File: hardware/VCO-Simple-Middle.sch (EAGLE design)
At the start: 14 parts

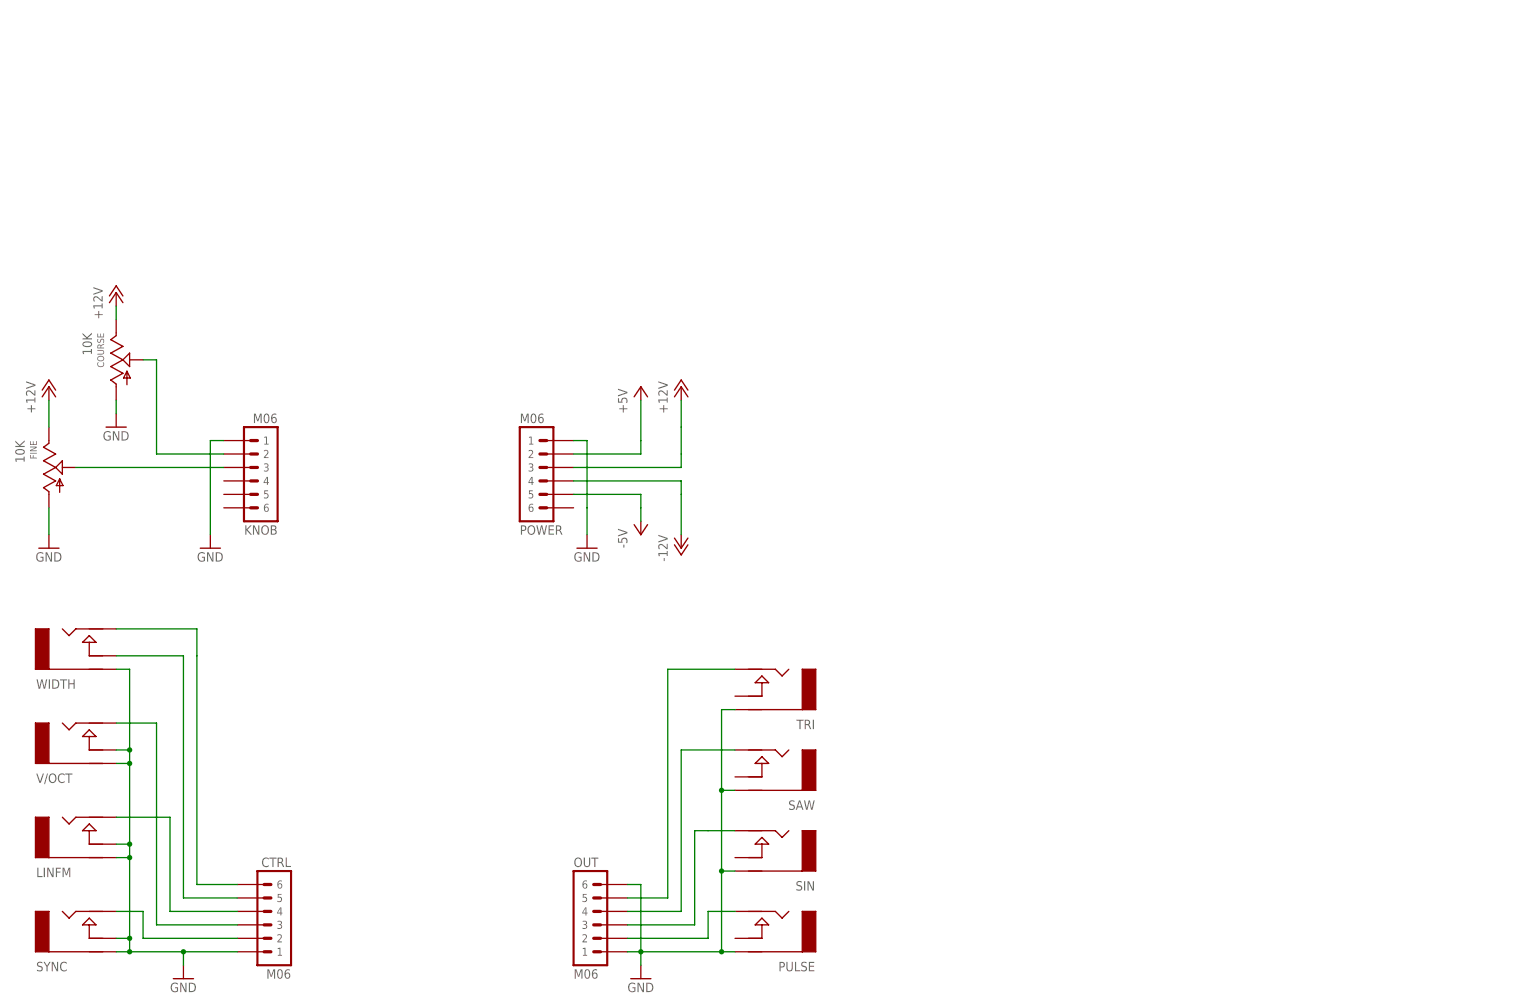
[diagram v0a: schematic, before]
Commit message: add page frames
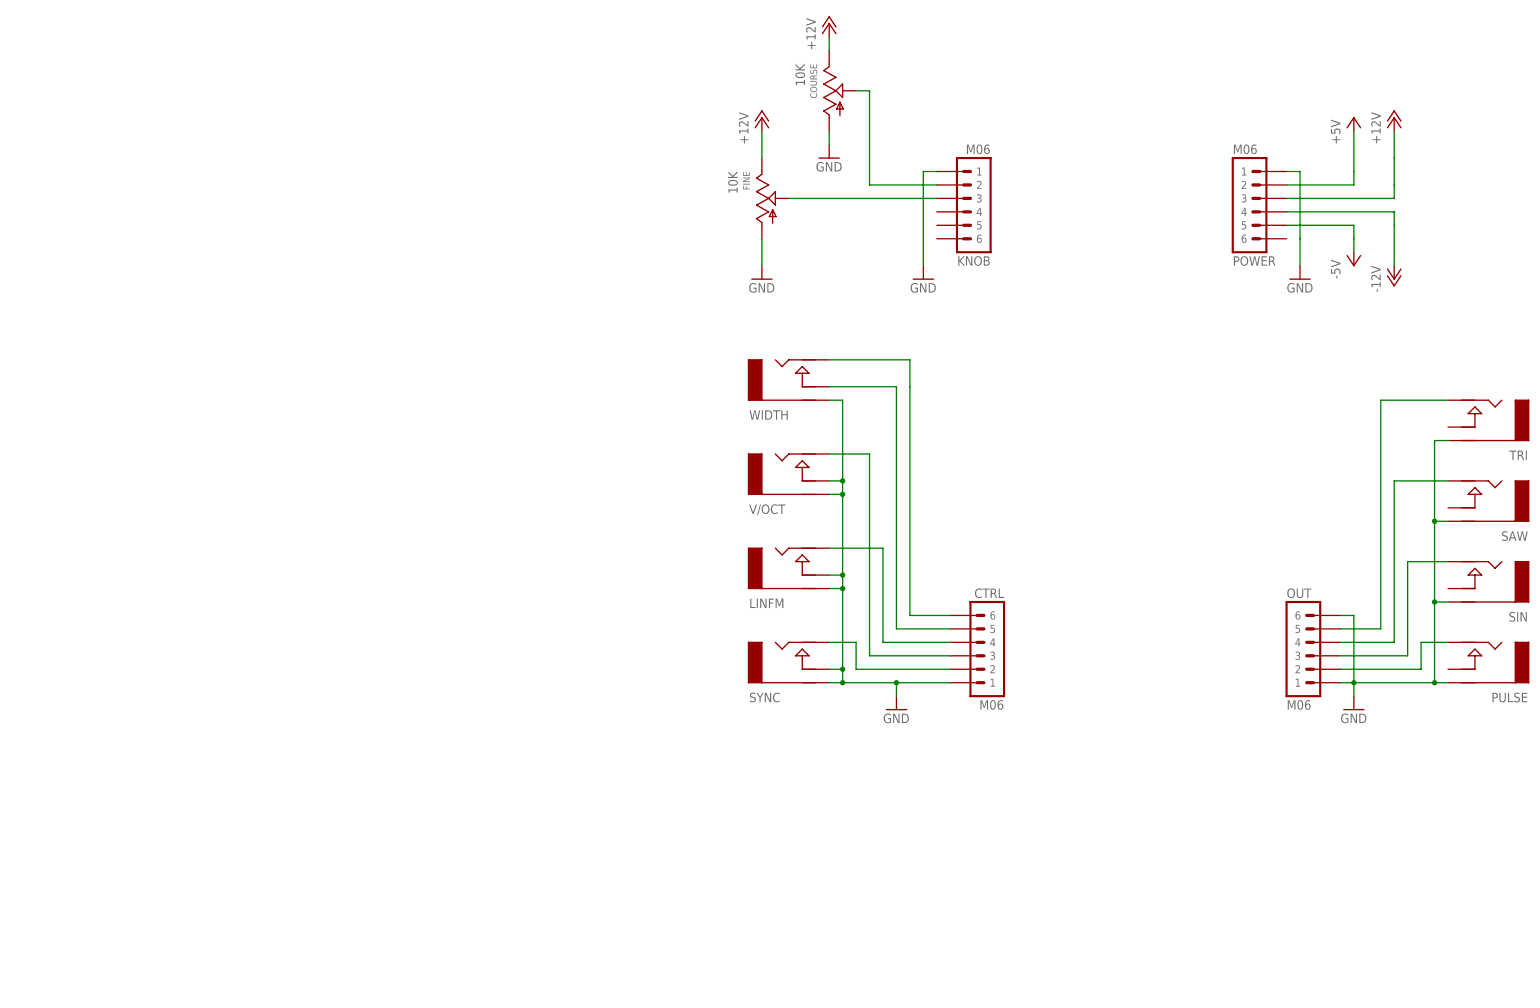
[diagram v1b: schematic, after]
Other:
- moved on the sheet: COURSE, CTRL, FINE, KNOB, LINFM, OUT, POWER, PULSE, SAW, SIN, SYNC, TRI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
